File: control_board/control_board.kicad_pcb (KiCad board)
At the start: 2 copper layers, 50.8 x 76.2 mm, 41 parts, among them J1 Conn_01x08_Male, K1 G5Q-1A, Q1 Q_NPN_BEC, U1 MC78M05_TO252, U2 TSR_1-24120, U3 74LS02, U4 74LS02, U5 Conn_01x08_Male

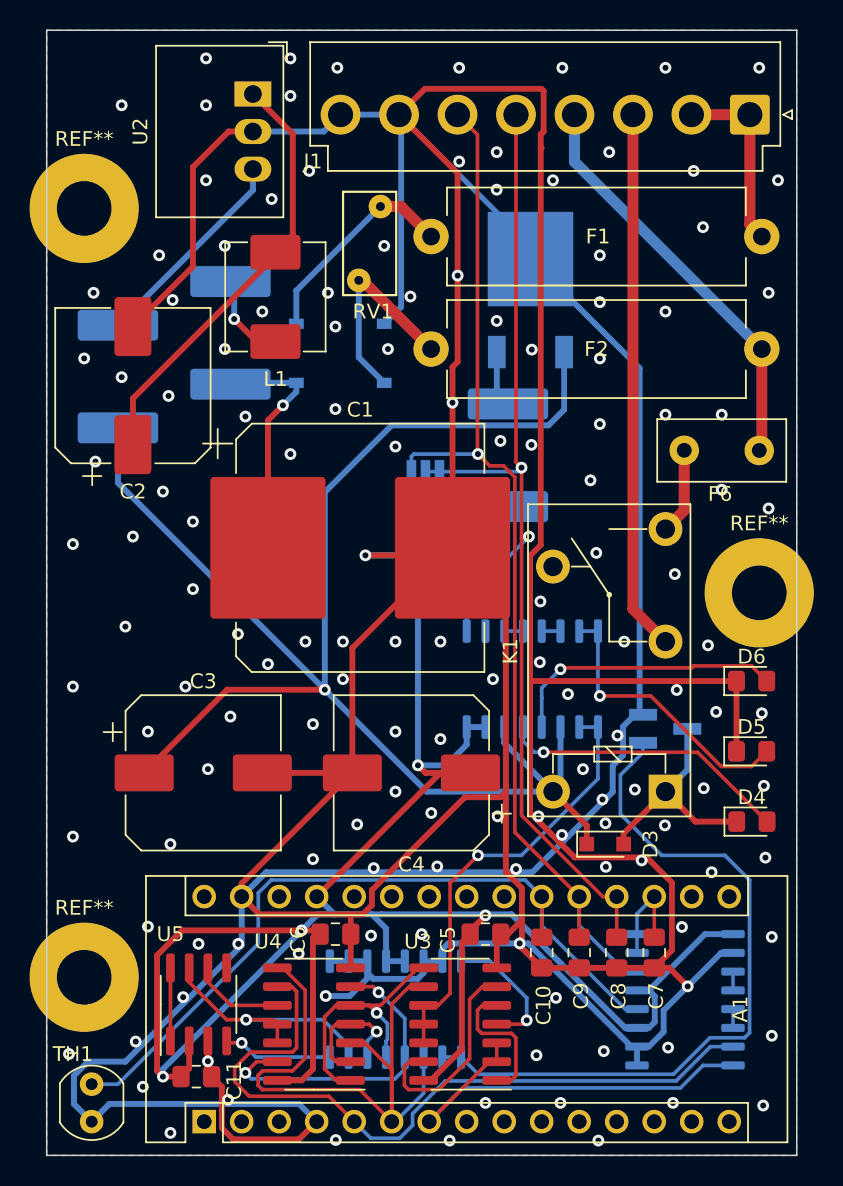
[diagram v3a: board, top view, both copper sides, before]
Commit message: Silkscreen cleanup, DRC check, few more vias
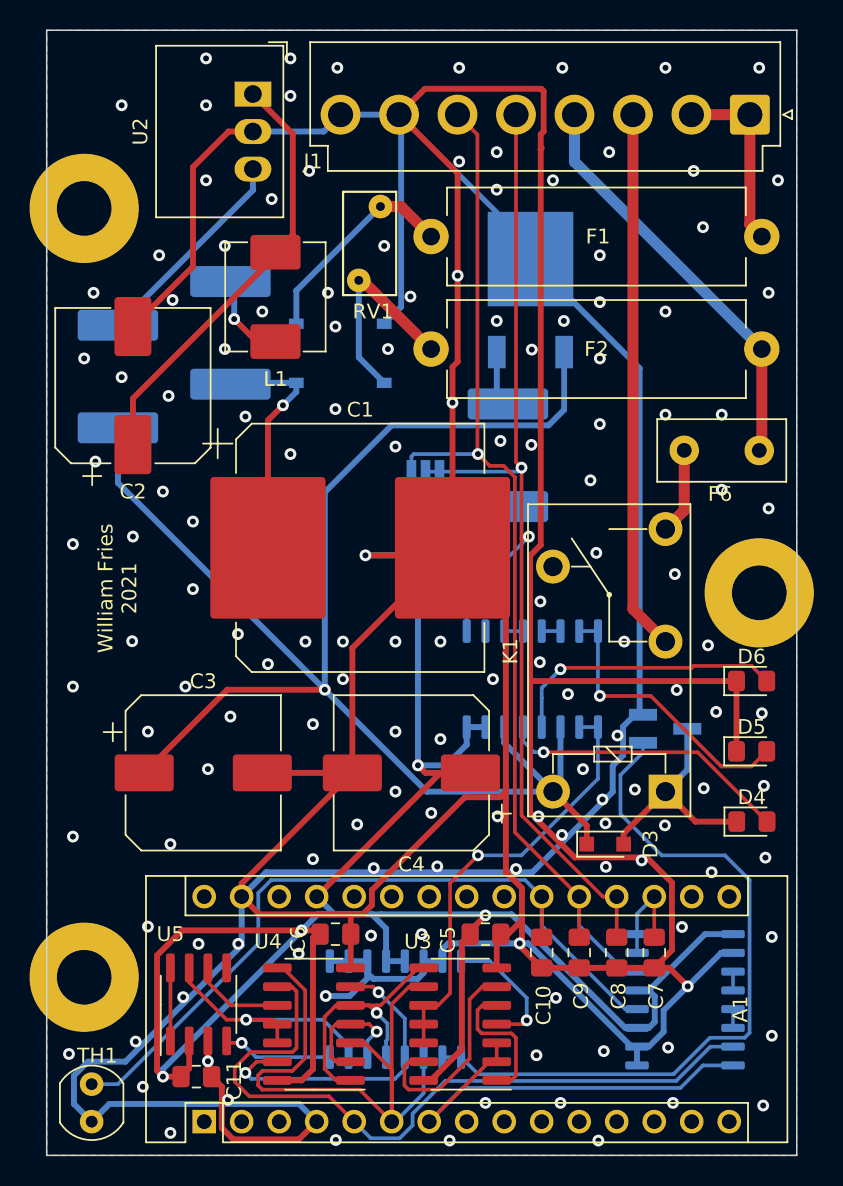
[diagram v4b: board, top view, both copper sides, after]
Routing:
- net GND: vias 144 -> 145
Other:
- board text added: "William Fries 2021"
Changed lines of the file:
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@@
   (general
     (thickness 1.6)
-    (drawings 11)
-    (tracks 628)
+    (drawings 12)
+    (tracks 629)
     (zones 0)
     (modules 41)
@@
     (38 B.Mask user hide)
     (39 F.Mask user hide)
-    (40 Dwgs.User user)
-    (41 Cmts.User user)
+    (40 Dwgs.User user hide)
+    (41 Cmts.User user hide)
     (42 Eco1.User user hide)
     (43 Eco2.User user hide)
@@
     (46 B.CrtYd user)
     (47 F.CrtYd user)
-    (48 B.Fab user)
-    (49 F.Fab user)
+    (48 B.Fab user hide)
+    (49 F.Fab user hide)
   )
   (setup
@@
     (tags "mounting hole 3.7mm")
     (attr virtual)
-    (fp_text reference REF** (at 0 -4.7) (layer F.SilkS)
+    (fp_text reference REF** (at 0 -4.7) (layer F.SilkS) hide
       (effects (font (size 1 1) (thickness 0.15)))
     )
     (fp_text value MountingHole_3.7mm_Pad (at 0 4.7) (layer F.Fab)
-      (effects (font (size 1 1) (thickness 0.15)))
-    )
-    (fp_text user %R (at 0.3 0) (layer F.Fab)
       (effects (font (size 1 1) (thickness 0.15)))
     )
     (fp_circle (center 0 0) (end 3.7 0) (layer Cmts.User) (width 0.15))
     (fp_circle (center 0 0) (end 3.95 0) (layer F.CrtYd) (width 0.05))
+    (fp_text user %R (at 0.3 0) (layer F.Fab)
+      (effects (font (size 1 1) (thickness 0.15)))
+    )
     (pad 1 thru_hole circle (at 0 0) (size 7.4 7.4) (drill 3.7) (layers *.Cu *.Mask))
   )
@@
     (tags "mounting hole 3.7mm")
     (attr virtual)
-    (fp_text reference REF** (at 0 -4.7) (layer F.SilkS)
+    (fp_text reference REF** (at 0 -4.7) (layer F.SilkS) hide
       (effects (font (size 1 1) (thickness 0.15)))
     )
@@
     (tags "mounting hole 3.7mm")
     (attr virtual)
-    (fp_text reference REF** (at 0 -4.7) (layer F.SilkS)
+    (fp_text reference REF** (at 0 -4.7) (layer F.SilkS) hide
       (effects (font (size 1 1) (thickness 0.15)))
     )
     (fp_text value MountingHole_3.7mm_Pad (at 0 4.7) (layer F.Fab)
-      (effects (font (size 1 1) (thickness 0.15)))
-    )
-    (fp_text user %R (at 0.3 0) (layer F.Fab)
       (effects (font (size 1 1) (thickness 0.15)))
     )
     (fp_circle (center 0 0) (end 3.7 0) (layer Cmts.User) (width 0.15))
     (fp_circle (center 0 0) (end 3.95 0) (layer F.CrtYd) (width 0.05))
+    (fp_text user %R (at 0.3 0) (layer F.Fab)
+      (effects (font (size 1 1) (thickness 0.15)))
+    )
     (pad 1 thru_hole circle (at 0 0) (size 7.4 7.4) (drill 3.7) (layers *.Cu *.Mask))
   )
@@
     (descr "Resistor, LDR 4.9x4.2mm")
     (tags "Resistor LDR4.9x4.2")
-    (fp_text reference TH1 (at -2.032 1.27 180) (layer F.SilkS)
+    (fp_text reference TH1 (at -1.9304 -0.381 180) (layer F.SilkS)
       (effects (font (size 1 1) (thickness 0.15)))
     )
@@
       (rotate (xyz 0 0 0))
     )
+  )
+  (gr_text "William Fries\n2021" (at 115.2906 61.9252 90) (layer F.SilkS)
+    (effects (font (size 1 1) (thickness 0.15)))
   )
   (gr_line (start 161.29 24.13) (end 161.29 100.33) (layer Edge.Cuts) (width 0.1))
@@
   (via (at 112.268 58.928) (size 0.8) (drill 0.4) (layers F.Cu B.Cu) (net 7))
   (via (at 112.268 68.58) (size 0.8) (drill 0.4) (layers F.Cu B.Cu) (net 7))
-  (via (at 115.824 64.516) (size 0.8) (drill 0.4) (layers F.Cu B.Cu) (net 7))
+  (via (at 116.2812 65.5066) (size 0.8) (drill 0.4) (layers F.Cu B.Cu) (net 7))
   (via (at 117.348 71.628) (size 0.8) (drill 0.4) (layers F.Cu B.Cu) (net 7))
   (via (at 119.888 68.58) (size 0.8) (drill 0.4) (layers F.Cu B.Cu) (net 7))
@@
   (segment (start 135.61699 88.37401) (end 132.60701 88.37401) (width 0.4) (layer B.Cu) (net 7))
   (via (at 132.461 85.4456) (size 0.8) (drill 0.4) (layers F.Cu B.Cu) (net 7))
+  (via (at 145.5166 43.815) (size 0.8) (drill 0.4) (layers F.Cu B.Cu) (net 7))
   (segment (start 146.558 82.804) (end 146.558 85.555) (width 0.25) (layer F.Cu) (net 8))
   (segment (start 149.672 87.884) (end 150.472 87.884) (width 0.25) (layer B.Cu) (net 8))

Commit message: Path and fill optimization
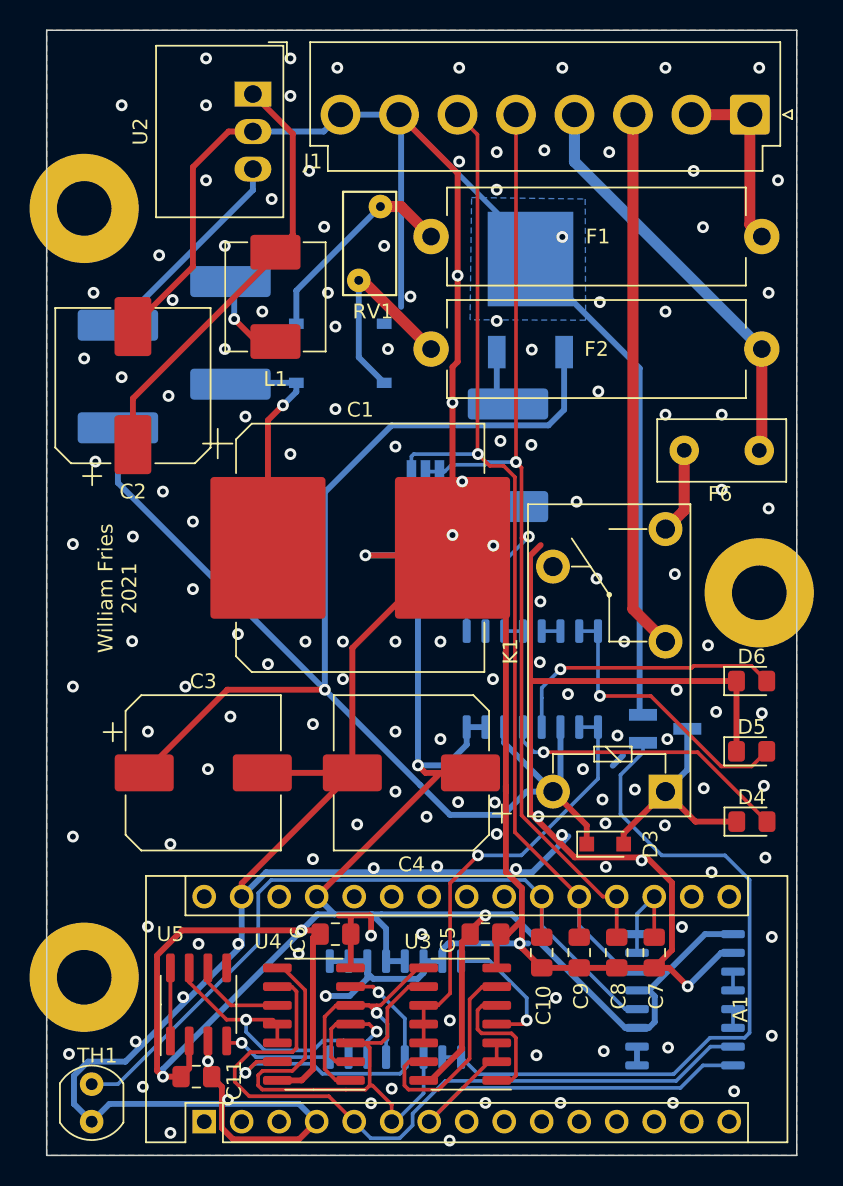
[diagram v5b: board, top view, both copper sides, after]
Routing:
- net GND: track 467.1 -> 379.8 mm, vias 145 -> 151
- net /sr_rst: track 44.6 -> 39.5 mm
- net +12V: track 107.0 -> 108.8 mm
- net Net-(RN2-Pad7): track 17.8 -> 18.9 mm

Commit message: Prepare for JLCPCB
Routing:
- net GND: vias 151 -> 150
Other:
- board text added: "JLCJLCJLCJLC"
- board text added: "William Fries 2021 Rev 1"
- board text removed: "William Fries 2021"
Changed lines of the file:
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@@
   (general
     (thickness 1.6)
-    (drawings 12)
-    (tracks 631)
+    (drawings 13)
+    (tracks 630)
     (zones 0)
     (modules 41)
@@
     )
   )
-  (gr_text "William Fries\n2021" (at 115.2906 61.9252 90) (layer F.SilkS)
+  (gr_text JLCJLCJLCJLC (at 122.0216 72.644) (layer B.SilkS)
+    (effects (font (size 1 1) (thickness 0.15)) (justify mirror))
+  )
+  (gr_text "William Fries\n2021\nRev 1" (at 115.9002 62.5094 90) (layer F.SilkS)
     (effects (font (size 1 1) (thickness 0.15)))
   )
@@
   (via (at 137.976 49.349) (size 0.8) (drill 0.4) (layers F.Cu B.Cu) (net 7))
   (via (at 133.35 38.735) (size 0.8) (drill 0.4) (layers F.Cu B.Cu) (net 7))
-  (via (at 129.54 41.91) (size 0.8) (drill 0.4) (layers F.Cu B.Cu) (net 7))
   (via (at 121.285 26.035) (size 0.8) (drill 0.4) (layers F.Cu B.Cu) (net 7))
   (via (at 127 26.035) (size 0.8) (drill 0.4) (layers F.Cu B.Cu) (net 7))
@@
   (via (at 118.11 39.37) (size 0.8) (drill 0.4) (layers F.Cu B.Cu) (net 7))
   (via (at 115.57 29.21) (size 0.8) (drill 0.4) (layers F.Cu B.Cu) (net 7))
-  (via (at 125.095 43.18) (size 0.8) (drill 0.4) (layers F.Cu B.Cu) (net 7))
   (via (at 122.555 45.72) (size 0.8) (drill 0.4) (layers F.Cu B.Cu) (net 7))
   (via (at 118.745 48.895) (size 0.8) (drill 0.4) (layers F.Cu B.Cu) (net 7))
@@
   (via (at 133.604 45.72) (size 0.8) (drill 0.4) (layers F.Cu B.Cu) (net 7))
   (via (at 135.128 42.164) (size 0.8) (drill 0.4) (layers F.Cu B.Cu) (net 7))
-  (via (at 130.048 44.196) (size 0.8) (drill 0.4) (layers F.Cu B.Cu) (net 7))
   (via (at 127 52.832) (size 0.8) (drill 0.4) (layers F.Cu B.Cu) (net 7))
   (via (at 113.792 53.34) (size 0.8) (drill 0.4) (layers F.Cu B.Cu) (net 7))
@@
   (via (at 152.527 72.136) (size 0.8) (drill 0.4) (layers F.Cu B.Cu) (net 7))
   (via (at 129.286 37.4396) (size 0.8) (drill 0.4) (layers F.Cu B.Cu) (net 7))
+  (via (at 129.5654 42.7228) (size 0.8) (drill 0.4) (layers F.Cu B.Cu) (net 7))
+  (via (at 125.3236 43.053) (size 0.8) (drill 0.4) (layers F.Cu B.Cu) (net 7))
   (segment (start 146.558 82.804) (end 146.558 85.555) (width 0.25) (layer F.Cu) (net 8))
   (segment (start 149.672 87.884) (end 150.472 87.884) (width 0.25) (layer B.Cu) (net 8))

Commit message: Finalize design
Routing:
- net +5V: track 156.9 -> 155.1 mm
- net GND: vias 150 -> 151
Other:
- board text added: "github.com/ FriesW/ sauna-controller"
- board text added: "https://github.com/FriesW/sauna-controller"

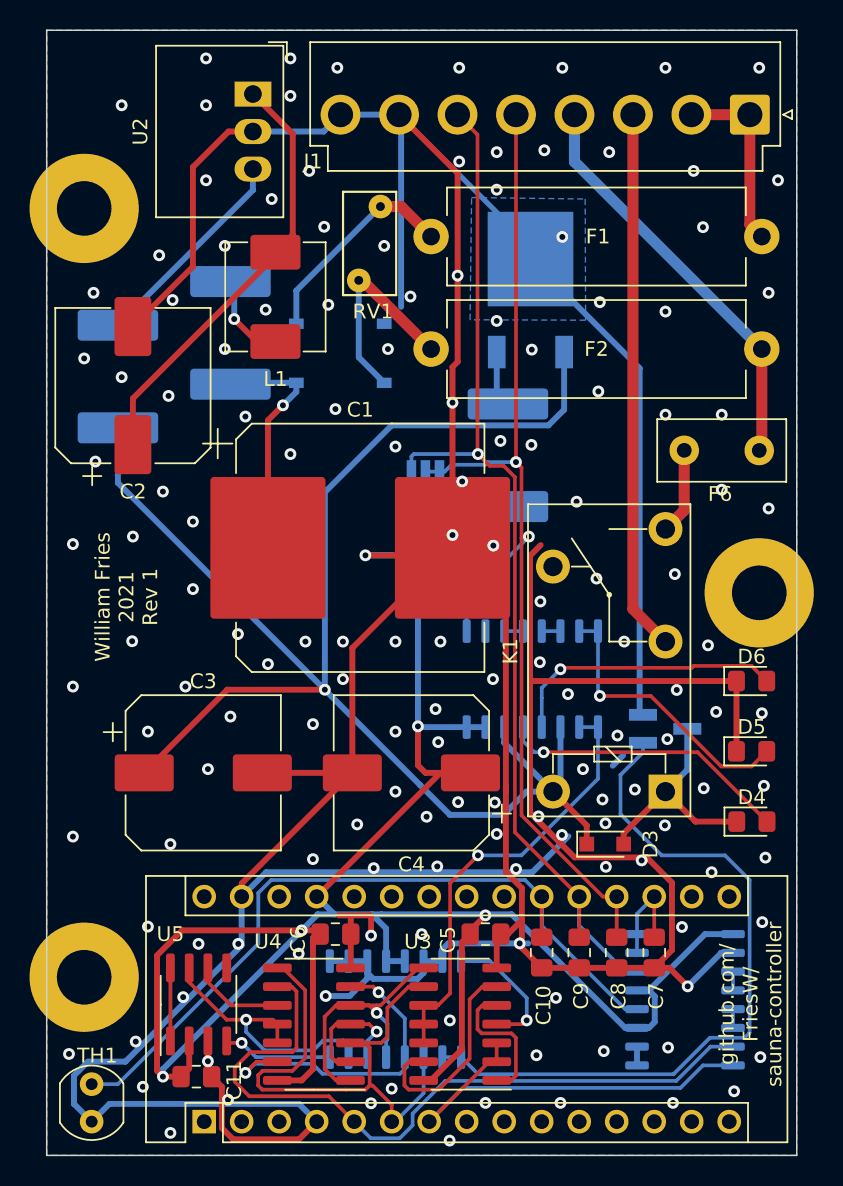
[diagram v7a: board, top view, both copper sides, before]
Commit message: Fix some DRC errors
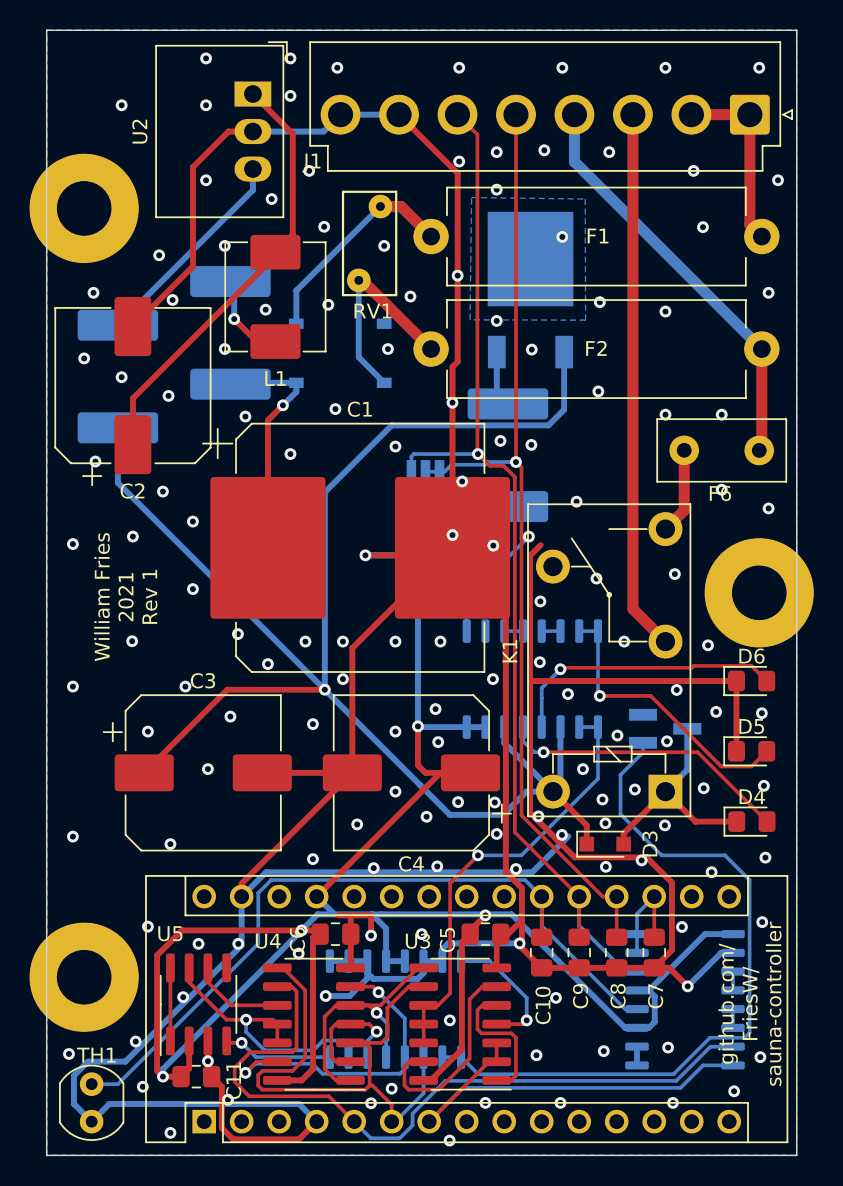
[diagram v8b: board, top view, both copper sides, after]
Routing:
- net GND: track 379.8 -> 318.6 mm
